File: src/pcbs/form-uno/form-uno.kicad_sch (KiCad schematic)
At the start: 121 parts, among them SW1 SW_Push, SW10 SW_Push, SW11 SW_Push, SW12 SW_Push, SW13 SW_Push, SW14 SW_Push, SW15 SW_Push, SW16 SW_Push, SW17 SW_Push, SW18 SW_Push, SW19 SW_Push, SW2 SW_Push, SW20 SW_Push, SW21 SW_Push, SW22 SW_Push, SW23 SW_Push, SW24 SW_Push, SW25 SW_Push, SW26 SW_Push, SW27 SW_Push, SW28 SW_Push, SW29 SW_Push, SW3 SW_Push, SW30 SW_Push, SW31 SW_Push, SW32 SW_Push, SW33 SW_Push, SW34 SW_Push, SW35 SW_Push, SW36 SW_Push, SW37 SW_Push, SW38 SW_Push, SW39 SW_Push, SW4 SW_Push, SW40 SW_Push, SW41 SW_Push, SW42 SW_Push, SW43 SW_Push, SW44 SW_Push, SW45 SW_Push, SW46 SW_Push, SW47 SW_Push, SW48 SW_Push, SW49 SW_Push, SW5 SW_Push, SW50 SW_Push, SW51 SW_Push, SW52 SW_Push, SW53 SW_Push, SW54 SW_Push, SW55 SW_Push, SW56 SW_Push, SW57 SW_Push, SW58 SW_Push, SW59 SW_Push, SW6 SW_Push, SW60 SW_Push, SW7 SW_Push, SW8 SW_Push, SW9 SW_Push, U1 rp2040-zero

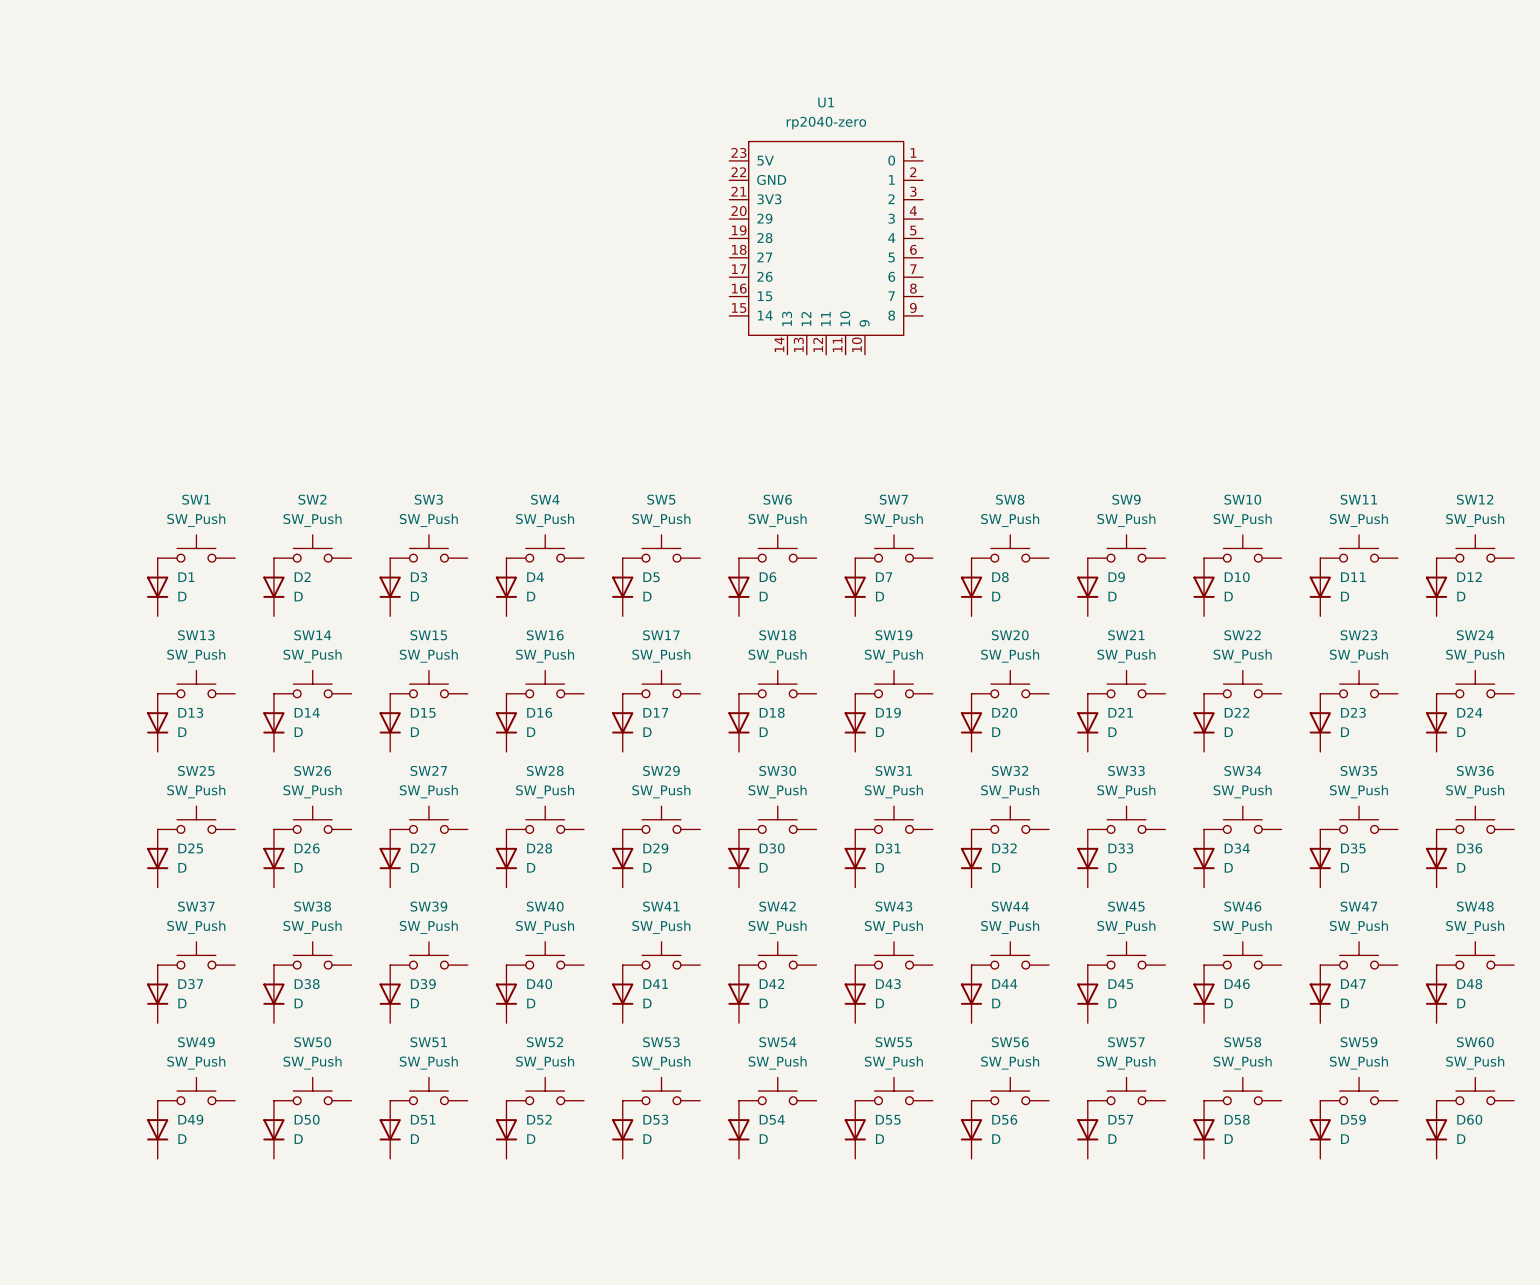
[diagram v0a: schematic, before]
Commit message: Route the board matrix
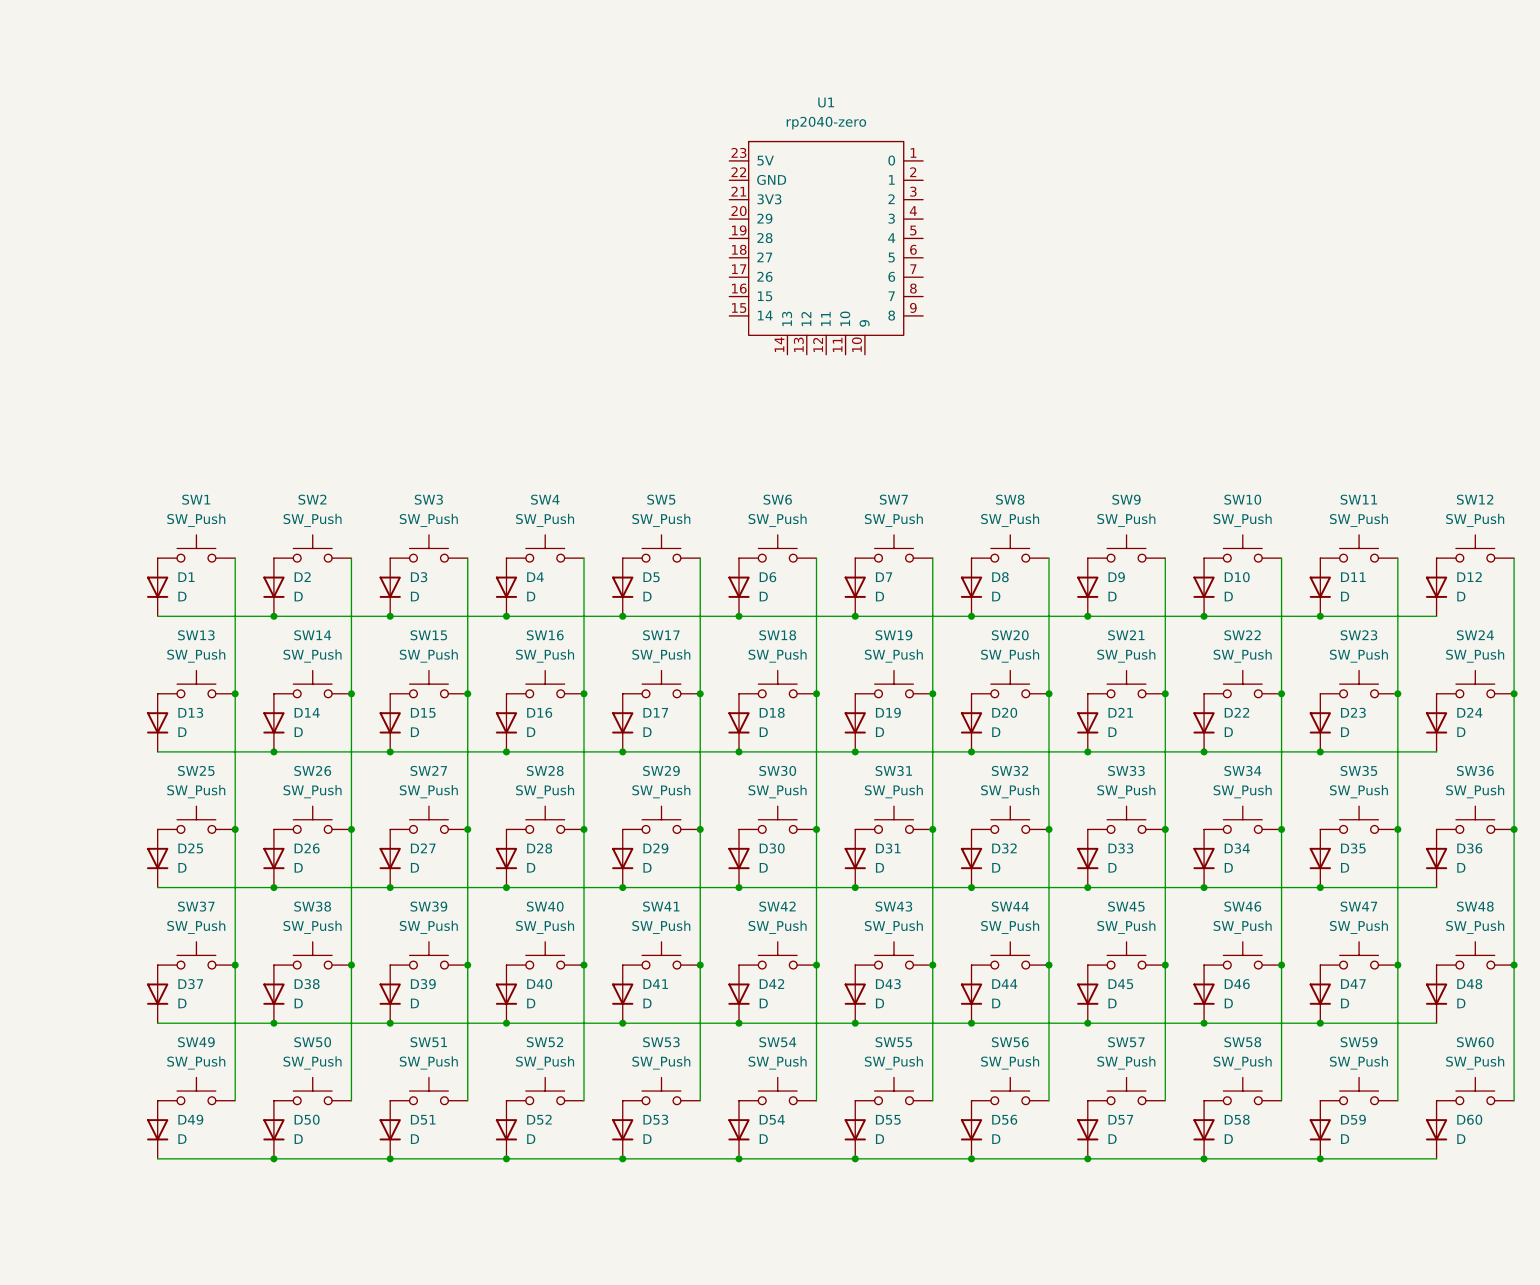
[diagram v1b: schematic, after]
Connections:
- net at SW16.2: now also SW28.2, SW4.2, SW40.2, SW52.2
- net at SW13.2: now also SW1.2, SW25.2, SW37.2, SW49.2
- net at D21.1 (K): now also D13.1 (K), D14.1 (K), D15.1 (K), D16.1 (K), D17.1 (K), D18.1 (K), D19.1 (K), D20.1 (K), D22.1 (K), D23.1 (K), D24.1 (K)
- net at SW54.2: now also SW18.2, SW30.2, SW42.2, SW6.2
- net at D4.1 (K): now also D1.1 (K), D10.1 (K), D11.1 (K), D12.1 (K), D2.1 (K), D3.1 (K), D5.1 (K), D6.1 (K), D7.1 (K), D8.1 (K), D9.1 (K)
- net at D31.1 (K): now also D25.1 (K), D26.1 (K), D27.1 (K), D28.1 (K), D29.1 (K), D30.1 (K), D32.1 (K), D33.1 (K), D34.1 (K), D35.1 (K), D36.1 (K)
- net at SW14.2: now also SW2.2, SW26.2, SW38.2, SW50.2
- net at D46.1 (K): now also D37.1 (K), D38.1 (K), D39.1 (K), D40.1 (K), D41.1 (K), D42.1 (K), D43.1 (K), D44.1 (K), D45.1 (K), D47.1 (K), D48.1 (K)
- net at SW8.2: now also SW20.2, SW32.2, SW44.2, SW56.2
- net at SW45.2: now also SW21.2, SW33.2, SW57.2, SW9.2
- net at SW24.2: now also SW12.2, SW36.2, SW48.2, SW60.2
- net at SW7.2: now also SW19.2, SW31.2, SW43.2, SW55.2
- net at SW35.2: now also SW11.2, SW23.2, SW47.2, SW59.2
- net at SW22.2: now also SW10.2, SW34.2, SW46.2, SW58.2
- net at SW15.2: now also SW27.2, SW3.2, SW39.2, SW51.2
- net at SW17.2: now also SW29.2, SW41.2, SW5.2, SW53.2
- net at D49.1 (K): now also D50.1 (K), D51.1 (K), D52.1 (K), D53.1 (K), D54.1 (K), D55.1 (K), D56.1 (K), D57.1 (K), D58.1 (K), D59.1 (K), D60.1 (K)

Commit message: Route the rows and cols to microcontroller
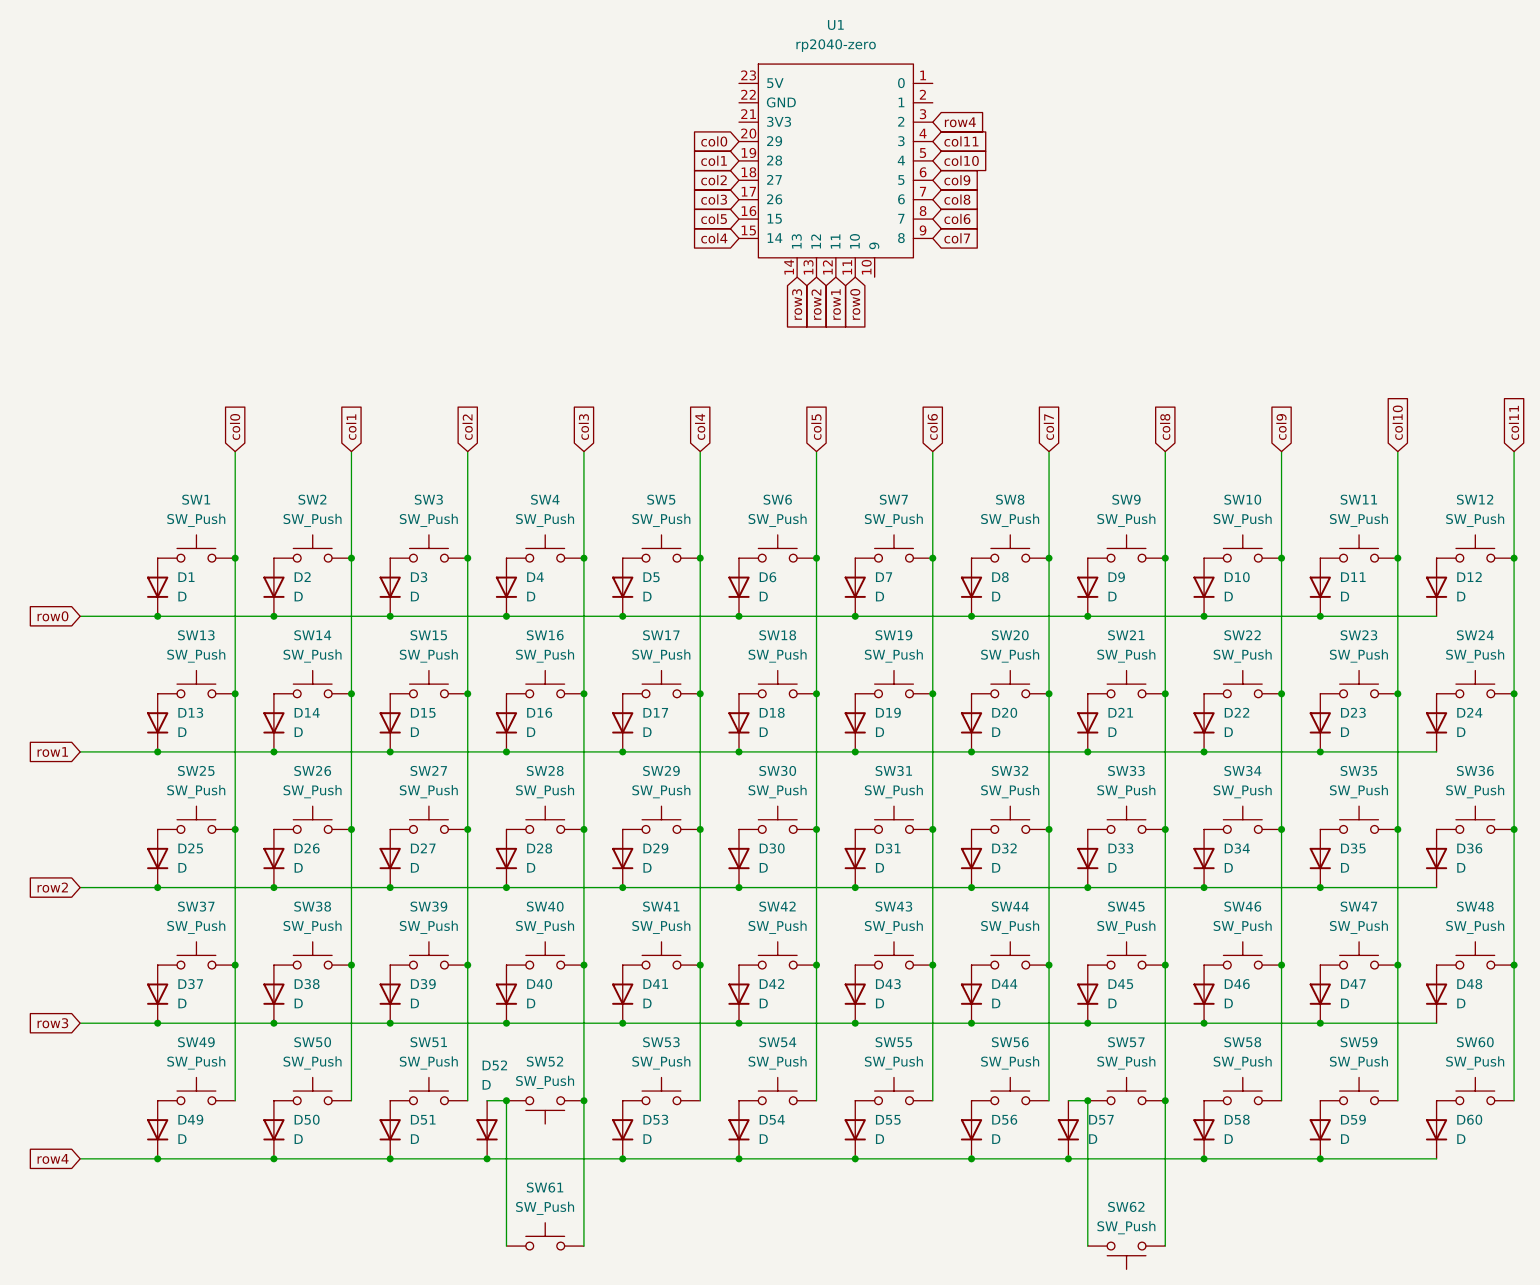
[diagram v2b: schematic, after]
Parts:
- added SW61, SW62: SW_Push, marbastlib-mx:SW_MX_HS_CPG151101S11_1u, symbol Switch:SW_Push
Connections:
- net col3: now reaches SW16.2, SW28.2, SW4.2, SW40.2
- net col3: now also SW52.1, U1.17 (26), SW61.2; no longer SW52.2
- net col0: now reaches SW1.2, SW13.2, SW25.2, SW37.2, SW49.2
- net col0: now also U1.20 (29)
- net row1: now reaches D13.1 (K), D14.1 (K), D15.1 (K), D16.1 (K), D17.1 (K), D18.1 (K), D19.1 (K), D20.1 (K), D21.1 (K), D22.1 (K), D23.1 (K), D24.1 (K)
- net row1: now also U1.12 (11)
- net col5: now reaches SW18.2, SW30.2, SW42.2, SW54.2, SW6.2
- net col5: now also U1.16 (15)
- net row0: now reaches D1.1 (K), D10.1 (K), D11.1 (K), D12.1 (K), D2.1 (K), D3.1 (K), D4.1 (K), D5.1 (K), D6.1 (K), D7.1 (K), D8.1 (K), D9.1 (K)
- net row0: now also U1.11 (10)
- net row2: now reaches D25.1 (K), D26.1 (K), D27.1 (K), D28.1 (K), D29.1 (K), D30.1 (K), D31.1 (K), D32.1 (K), D33.1 (K), D34.1 (K), D35.1 (K), D36.1 (K)
- net row2: now also U1.13 (12)
- net col1: now reaches SW14.2, SW2.2, SW26.2, SW38.2, SW50.2
- net col1: now also U1.19 (28)
- net row3: now reaches D37.1 (K), D38.1 (K), D39.1 (K), D40.1 (K), D41.1 (K), D42.1 (K), D43.1 (K), D44.1 (K), D45.1 (K), D46.1 (K), D47.1 (K), D48.1 (K)
- net row3: now also U1.14 (13)
- net col7: now reaches SW20.2, SW32.2, SW44.2, SW56.2, SW8.2
- net col7: now also U1.9 (8)
- net col8: now reaches SW21.2, SW33.2, SW45.2, SW57.2, SW9.2
- net col8: now also U1.7 (6), SW62.1
- net col11: now reaches SW12.2, SW24.2, SW36.2, SW48.2, SW60.2
- net col11: now also U1.4 (3)
- net col6: now reaches SW19.2, SW31.2, SW43.2, SW55.2, SW7.2
- net col6: now also U1.8 (7)
- net col10: now reaches SW11.2, SW23.2, SW35.2, SW47.2, SW59.2
- net col10: now also U1.5 (4)
- net col9: now reaches SW10.2, SW22.2, SW34.2, SW46.2, SW58.2
- net col9: now also U1.6 (5)
- net col2: now reaches SW15.2, SW27.2, SW3.2, SW39.2, SW51.2
- net col2: now also U1.18 (27)
- net col4: now reaches SW17.2, SW29.2, SW41.2, SW5.2, SW53.2
- net col4: now also U1.15 (14)
- net row4: now reaches D49.1 (K), D50.1 (K), D51.1 (K), D52.1 (K), D53.1 (K), D54.1 (K), D55.1 (K), D56.1 (K), D57.1 (K), D58.1 (K), D59.1 (K), D60.1 (K)
- net row4: now also U1.3 (2)
- net at D57.2 (A), SW57.1: now also SW62.2
- net at D52.2 (A): now also SW52.2, SW61.1; no longer SW52.1
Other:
- moved on the sheet: D52, D57, SW52, U1

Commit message: Update rp2040 tiny footprint
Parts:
- U1: footprint mcu:rp2040-zero-smd -> rp2040-tiny:rp2040-tiny
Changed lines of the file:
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@@
 			)
 		)
-		(property "Footprint" "mcu:rp2040-zero-smd"
+		(property "Footprint" "rp2040-tiny:rp2040-tiny"
 			(at 120.65 19.05 0)
 			(effects
